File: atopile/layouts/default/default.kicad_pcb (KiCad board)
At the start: 4 copper layers, 78 x 60 mm, 86 parts

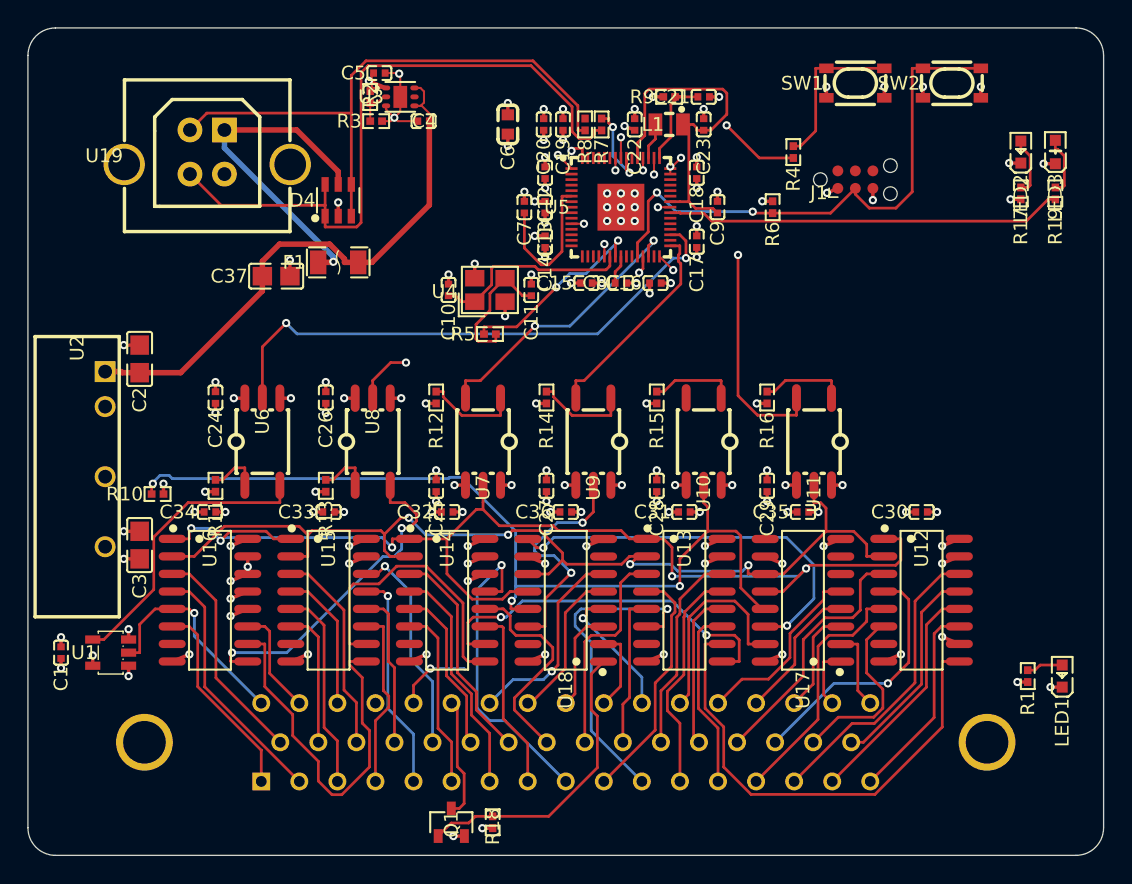
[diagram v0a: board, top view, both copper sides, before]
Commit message: atopile: RP2354A decoupling caps 0.9 mm further out, for pin escape
The caps sat 1.2 mm from the QFN pin tips, and with their via drops the
channel could not hold the south-side signals (SCK, CLK, MISO, N_RESET
kept displacing each other). Layout reset to the new placement and via
drops, unrouted, for the next Freerouting run.

Co-Authored-By: Claude Opus 5.5 <noreply@anthropic.com>
Claude-Session: https://claude.ai/code/session_01NqBEt2iCuw3VMJkgzgPtpr
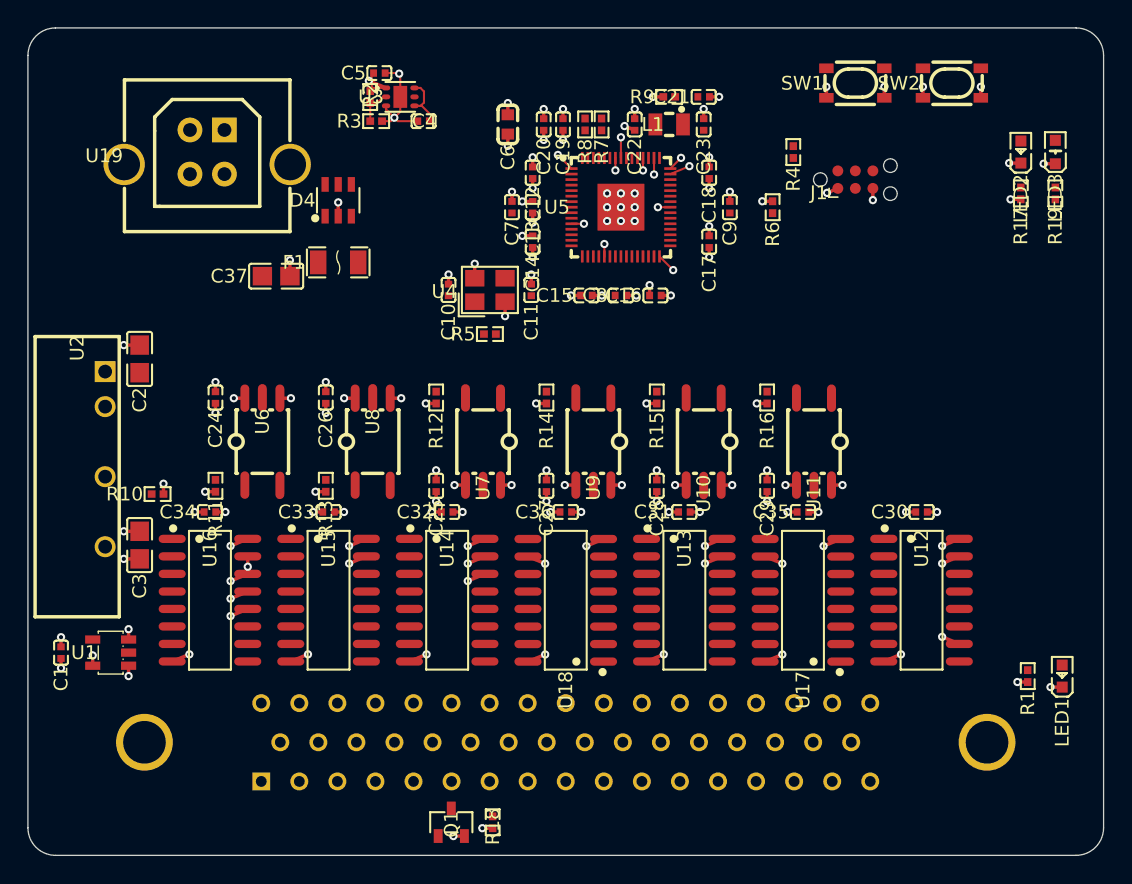
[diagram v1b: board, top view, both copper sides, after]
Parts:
- moved C15 0.90 mm to (1.50, -10.6)
- moved C16 0.90 mm to (6.50, -10.6)
- moved C17 0.90 mm to (10.4, -14.5)
- moved C18 0.90 mm to (10.4, -19.5)
- moved C8 0.90 mm to (4.00, -10.6)
- moved C9 0.90 mm to (11.9, -17.0)
- moved C12 0.90 mm to (-2.40, -19.5)
- moved C13 0.90 mm to (-2.40, -17.0)
- moved C14 0.90 mm to (-2.40, -14.5)
- moved C7 0.90 mm to (-3.90, -17.0)
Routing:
- net LATCH_ISO: track 82.7 -> 0.00 mm, vias 5 -> 0
- net SCK_ISO: track 74.7 -> 0.00 mm, vias 4 -> 0
- net OE_N_ISO: track 65.0 -> 0.00 mm, vias 3 -> 0
- net DATA_P: track 48.7 -> 0.00 mm
- net DATA_N: track 42.9 -> 0.00 mm
- net N_RESET: track 40.4 -> 0.00 mm, vias 2 -> 0
- net DRDY: track 40.3 -> 0.00 mm, vias 2 -> 0
- net +1V1: track 38.9 -> 0.00 mm
- net +5V: track 41.3 -> 3.86 mm
- net SI_CHAIN_4: track 35.4 -> 0.00 mm
- net SO_CHAIN_1: track 29.0 -> 0.00 mm, vias 2 -> 0
- net STATUS_LED: track 28.8 -> 0.00 mm
- net SI_CHAIN_1: track 27.2 -> 0.00 mm
- net SI_CHAIN_3: track 27.1 -> 0.00 mm, vias 2 -> 0
- net VBUS: track 24.4 -> 0.00 mm, vias 1 -> 0
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
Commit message: atopile: import Freerouting run 6 (wider MCU escape channels)
Freerouting 2.1 (patched) ended at 3 incomplete connections, no
clearance violations; finish_routes.py is closing the rest.

Co-Authored-By: Claude Opus 5.5 <noreply@anthropic.com>
Claude-Session: https://claude.ai/code/session_01NqBEt2iCuw3VMJkgzgPtpr
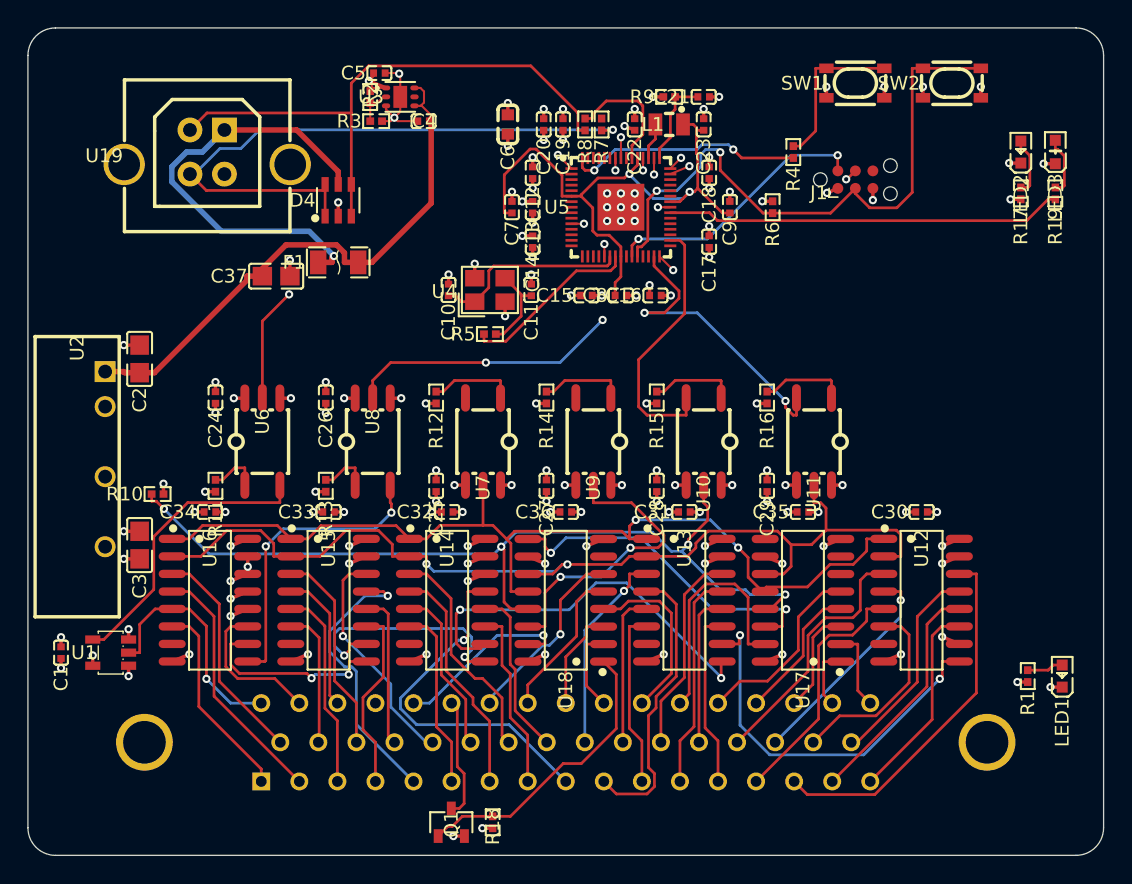
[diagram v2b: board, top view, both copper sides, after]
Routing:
- net SCK_ISO: track 0.00 -> 73.7 mm, vias 0 -> 2
- net LATCH_ISO: track 0.00 -> 70.0 mm, vias 0 -> 2
- net OE_N_ISO: track 0.00 -> 64.2 mm, vias 0 -> 4
- net DATA_P: track 0.00 -> 45.4 mm, vias 0 -> 1
- net N_RESET: track 0.00 -> 44.4 mm, vias 0 -> 2
- net +1V1: track 0.00 -> 43.5 mm, vias 0 -> 2
- net DATA_N: track 0.00 -> 42.0 mm
- net +5V: track 3.86 -> 41.0 mm
- net VBUS: track 0.00 -> 31.9 mm, vias 0 -> 1
- net STATUS_LED: track 0.00 -> 28.8 mm
- net SI_CHAIN_3: track 0.00 -> 28.8 mm, vias 0 -> 2
- net SI_CHAIN_4: track 0.00 -> 28.7 mm, vias 0 -> 2
- net SKB15_D2_4: track 0.00 -> 26.5 mm
- net SKB09_D4_1: track 0.00 -> 26.2 mm, vias 0 -> 1
- net SO_CHAIN_1: track 0.00 -> 24.7 mm, vias 0 -> 2
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
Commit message: atopile: USB series resistors swapped and turned so DP/DM do not cross
DP (pin 52) is west of DM (pin 51), but DP's resistor sat east of DM's,
and both had their MCU-side pad facing away from the MCU, so the pair had
to cross. Layout reset to the new placement and via drops, unrouted, for
the next Freerouting run.

Co-Authored-By: Claude Opus 5.5 <noreply@anthropic.com>
Claude-Session: https://claude.ai/code/session_01NqBEt2iCuw3VMJkgzgPtpr
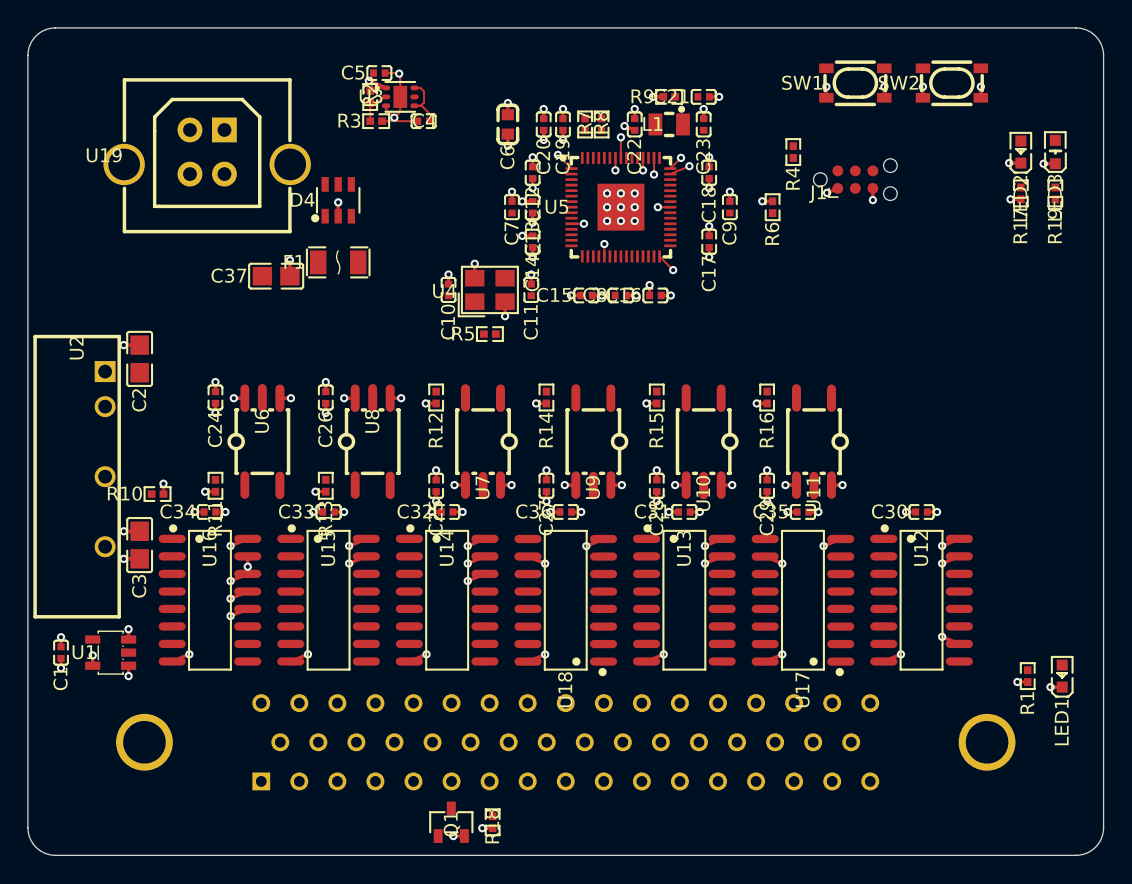
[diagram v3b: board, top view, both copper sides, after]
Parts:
- moved R7 1.20 mm to (1.40, -23.0), turned to 270 degrees
- moved R8 1.20 mm to (2.60, -23.0), turned to 270 degrees
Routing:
- net SCK_ISO: track 73.7 -> 0.00 mm, vias 2 -> 0
- net LATCH_ISO: track 70.0 -> 0.00 mm, vias 2 -> 0
- net OE_N_ISO: track 64.2 -> 0.00 mm, vias 4 -> 0
- net DATA_P: track 45.4 -> 0.00 mm, vias 1 -> 0
- net N_RESET: track 44.4 -> 0.00 mm, vias 2 -> 0
- net +1V1: track 43.5 -> 0.00 mm, vias 2 -> 0
- net DATA_N: track 42.0 -> 0.00 mm
- net +5V: track 41.0 -> 3.86 mm
- net VBUS: track 31.9 -> 0.00 mm, vias 1 -> 0
- net STATUS_LED: track 28.8 -> 0.00 mm
- net SI_CHAIN_3: track 28.8 -> 0.00 mm, vias 2 -> 0
- net SI_CHAIN_4: track 28.7 -> 0.00 mm, vias 2 -> 0
- net SKB15_D2_4: track 26.5 -> 0.00 mm
- net SKB09_D4_1: track 26.2 -> 0.00 mm, vias 1 -> 0
- net SO_CHAIN_1: track 24.7 -> 0.00 mm, vias 2 -> 0
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
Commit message: atopile: import Freerouting run 7 (after the USB resistor fix)
Freerouting 2.1 (patched) ended at 2 incomplete connections, no
clearance violations; finish_routes.py is closing the rest.

Co-Authored-By: Claude Opus 5.5 <noreply@anthropic.com>
Claude-Session: https://claude.ai/code/session_01NqBEt2iCuw3VMJkgzgPtpr
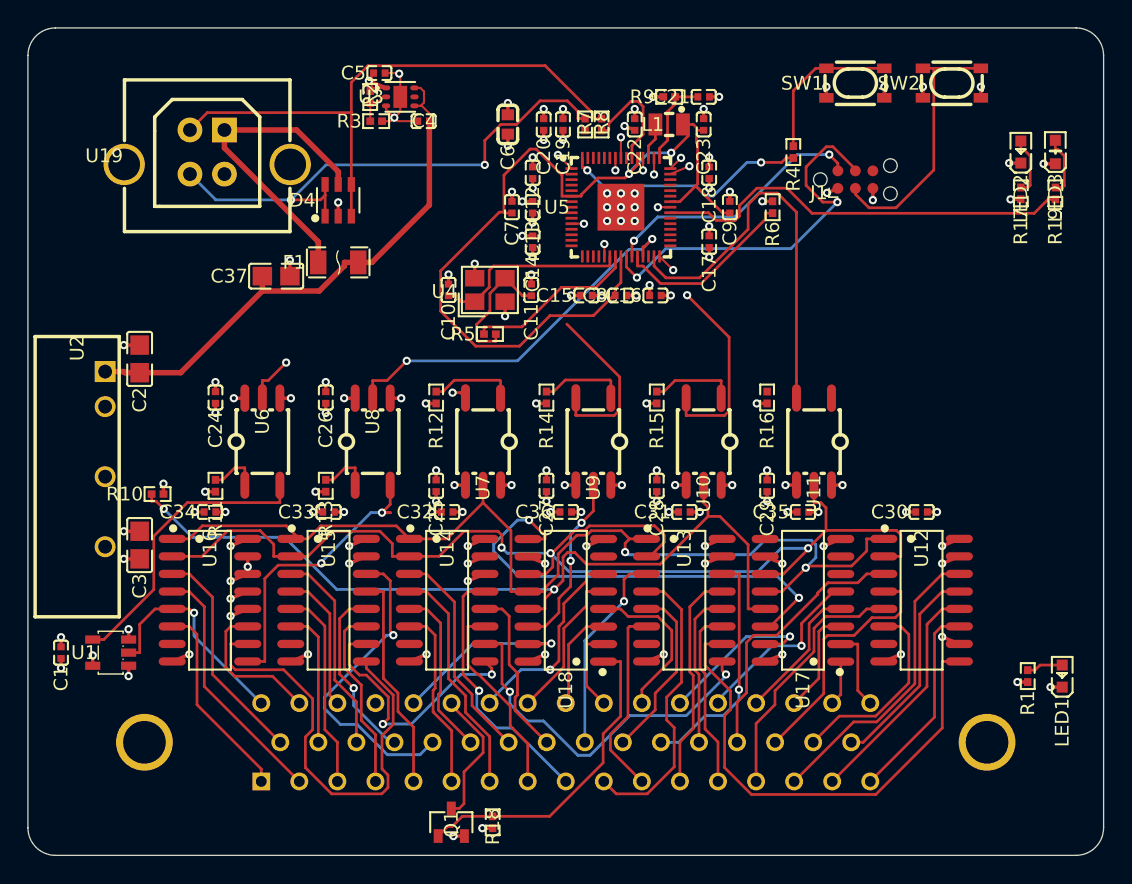
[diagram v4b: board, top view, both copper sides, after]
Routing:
- net SCK_ISO: track 0.00 -> 86.1 mm, vias 0 -> 3
- net LATCH_ISO: track 0.00 -> 75.5 mm, vias 0 -> 2
- net +1V1: track 0.00 -> 63.0 mm, vias 0 -> 2
- net OE_N_ISO: track 0.00 -> 62.4 mm, vias 0 -> 2
- net DATA_N: track 0.00 -> 42.3 mm
- net DATA_P: track 0.00 -> 39.2 mm, vias 0 -> 2
- net +5V: track 3.86 -> 39.9 mm
- net SI_CHAIN_4: track 0.00 -> 35.8 mm
- net SO_CHAIN_1: track 0.00 -> 33.8 mm, vias 0 -> 2
- net N_RESET: track 0.00 -> 32.6 mm
- net SI_CHAIN_1: track 0.00 -> 32.4 mm
- net STATUS_LED: track 0.00 -> 30.7 mm
- net SCK: track 0.00 -> 29.0 mm
- net CLK: track 0.00 -> 27.7 mm, vias 0 -> 2
- net MISO: track 0.00 -> 27.4 mm, vias 0 -> 2
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
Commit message: atopile: plane_vias.py no-via area for the USB pair; strap fallback
- NO_VIA_AREAS keeps via drops out of the DP/DM channel between RP2354A
  pins 51/52 and R7/R8 (two +3V3 drops there blocked the pair)
- a pin with no free via spot is strapped to an adjacent same-net pin
  that has one (RP2354A pin 53 -> 54)
Layout reset to the new via drops, unrouted, for the next run.

Co-Authored-By: Claude Opus 5.5 <noreply@anthropic.com>
Claude-Session: https://claude.ai/code/session_01NqBEt2iCuw3VMJkgzgPtpr
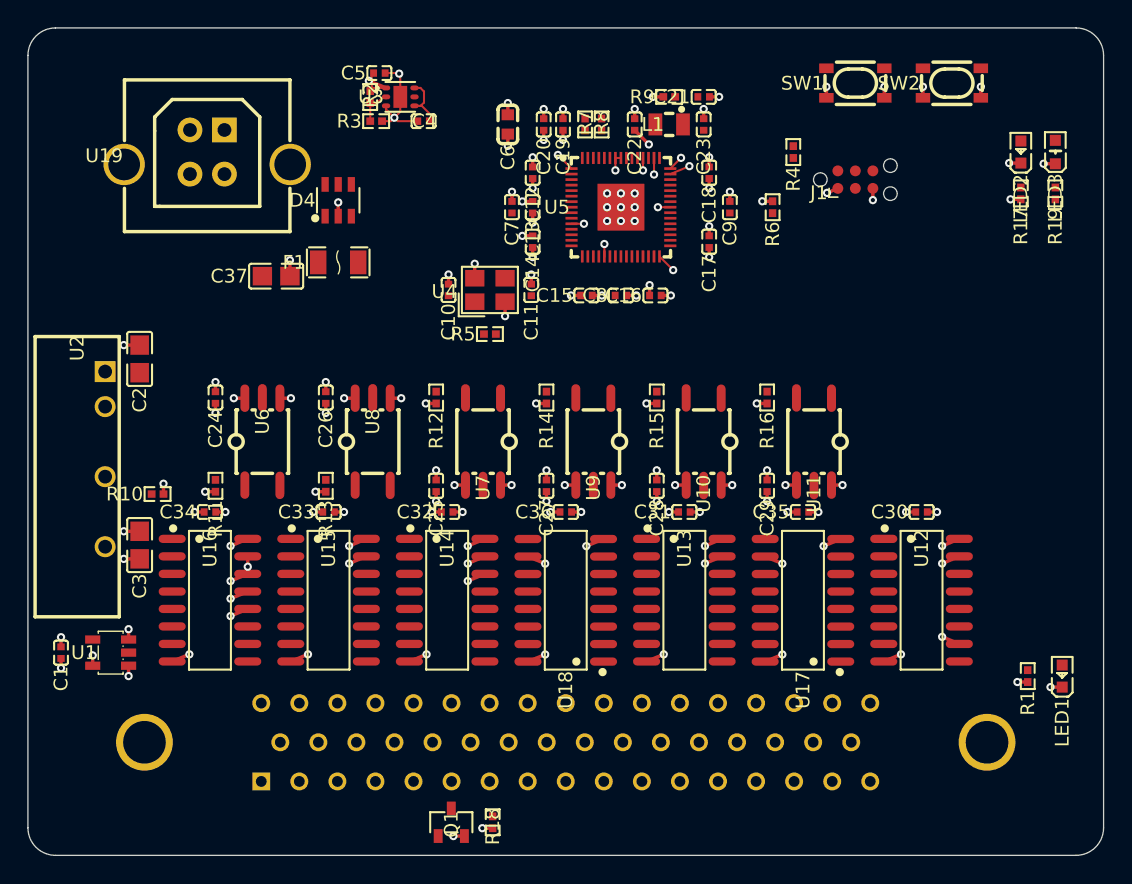
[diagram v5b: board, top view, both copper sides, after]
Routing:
- net SCK_ISO: track 86.1 -> 0.00 mm, vias 3 -> 0
- net LATCH_ISO: track 75.5 -> 0.00 mm, vias 2 -> 0
- net +1V1: track 63.0 -> 0.00 mm, vias 2 -> 0
- net OE_N_ISO: track 62.4 -> 0.00 mm, vias 2 -> 0
- net DATA_N: track 42.3 -> 0.00 mm
- net DATA_P: track 39.2 -> 0.00 mm, vias 2 -> 0
- net +5V: track 39.9 -> 3.86 mm
- net SI_CHAIN_4: track 35.8 -> 0.00 mm
- net SO_CHAIN_1: track 33.8 -> 0.00 mm, vias 2 -> 0
- net N_RESET: track 32.6 -> 0.00 mm
- net SI_CHAIN_1: track 32.4 -> 0.00 mm
- net STATUS_LED: track 30.7 -> 0.00 mm
- net SCK: track 29.0 -> 0.00 mm
- net CLK: track 27.7 -> 0.00 mm, vias 2 -> 0
- net MISO: track 27.4 -> 0.00 mm, vias 2 -> 0
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
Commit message: atopile: import Freerouting run 8 (USB channel kept clear)
Freerouting 2.1 (patched) ended at 3 incomplete connections, no
clearance violations; finish_routes.py is closing the rest.

Co-Authored-By: Claude Opus 5.5 <noreply@anthropic.com>
Claude-Session: https://claude.ai/code/session_01NqBEt2iCuw3VMJkgzgPtpr
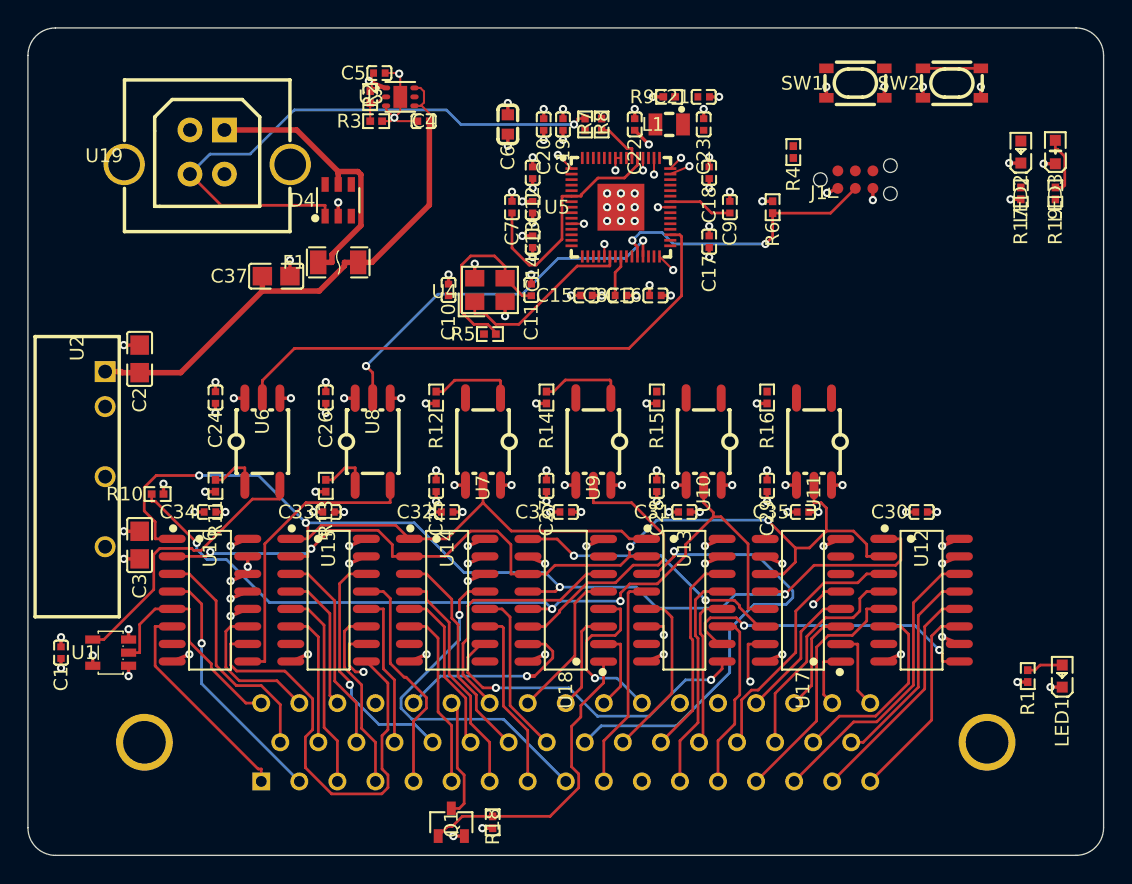
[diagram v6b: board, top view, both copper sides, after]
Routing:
- net LATCH_ISO: track 0.00 -> 103.9 mm, vias 0 -> 4
- net SCK_ISO: track 0.00 -> 72.6 mm, vias 0 -> 4
- net OE_N_ISO: track 0.00 -> 61.9 mm, vias 0 -> 3
- net DATA_P: track 0.00 -> 42.8 mm, vias 0 -> 1
- net DRDY: track 0.00 -> 39.4 mm
- net +5V: track 3.86 -> 39.9 mm
- net SKB26_POL_POS: track 0.00 -> 35.9 mm, vias 0 -> 1
- net SI_CHAIN_1: track 0.00 -> 32.0 mm
- net MISO: track 0.00 -> 27.5 mm, vias 0 -> 2
- net SKB09_D4_1: track 0.00 -> 25.8 mm, vias 0 -> 1
- net +1V1: track 0.00 -> 25.2 mm
- net N_RESET: track 0.00 -> 24.9 mm, vias 0 -> 2
- net SI_CHAIN_3: track 0.00 -> 24.9 mm, vias 0 -> 2
- net SI_CHAIN_4: track 0.00 -> 22.4 mm, vias 0 -> 2
- net SAMPLE_CONTACT_GATE: track 0.00 -> 22.0 mm
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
